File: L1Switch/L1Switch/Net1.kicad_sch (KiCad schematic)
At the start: 66 parts, among them J6 Conn_01x07_Male, U8 VSC8658

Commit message: Most signals routed.
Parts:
- renumbered C206 to C291, C207 to C292, C208 to C293, C209 to C294, C210 to C295, C211 to C296, C212 to C297, C213 to C298, C214 to C299, C215 to C300, C216 to C301, C217 to C302, C218 to C303, C219 to C304, C220 to C305, C221 to C306, C222 to C307, C223 to C308, C224 to C309, C225 to C310, C226 to C311, C227 to C312, C228 to C313, C229 to C314, C230 to C315, C231 to C316, C232 to C317, C233 to C318, C234 to C319, C235 to C320, C236 to C321, C237 to C322, C238 to C323, C239 to C324, C240 to C325, C241 to C326, C242 to C327, C243 to C328, C244 to C329, C245 to C330, C246 to C331, C247 to C332, C248 to C333, C249 to C334, C250 to C335, FB3 to FB4, J6 to J8, R138 to R197, R139 to R198, R140 to R199, R141 to R200, R142 to R201, R143 to R202, R144 to R203, R145 to R204, R146 to R205, R147 to R206, R148 to R207, U8 to U9

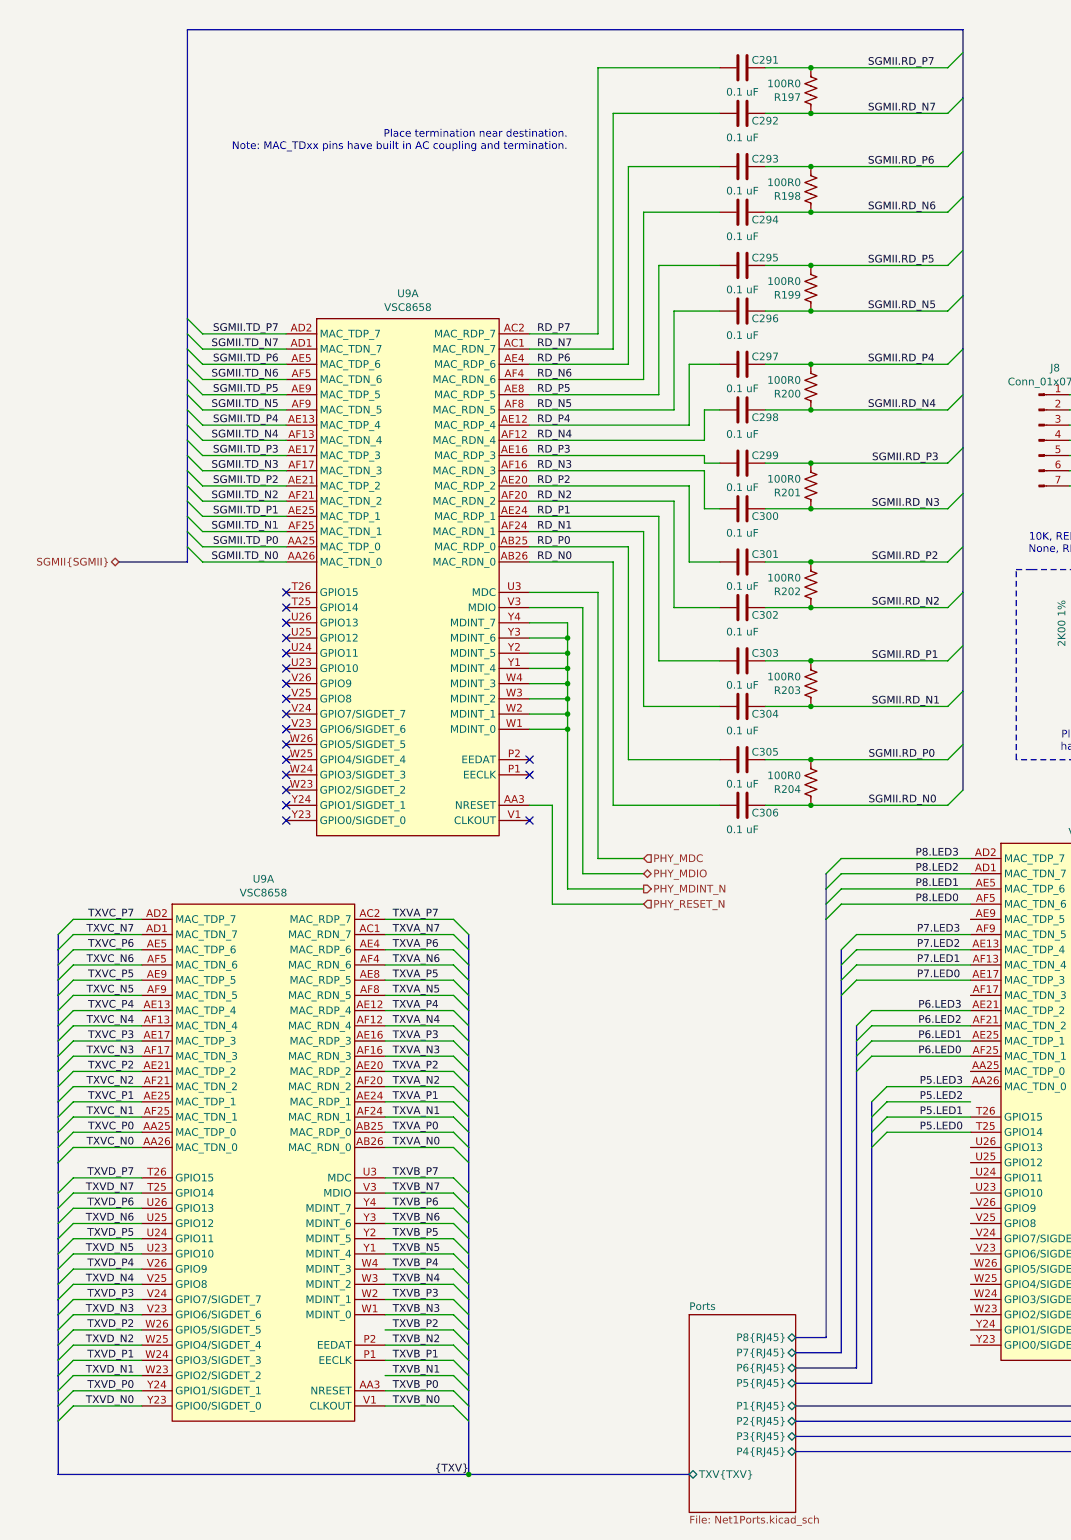
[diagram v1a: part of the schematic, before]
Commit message: Switch to XC7A35T. Update some layout constraints for 4pcb.com capabilities.
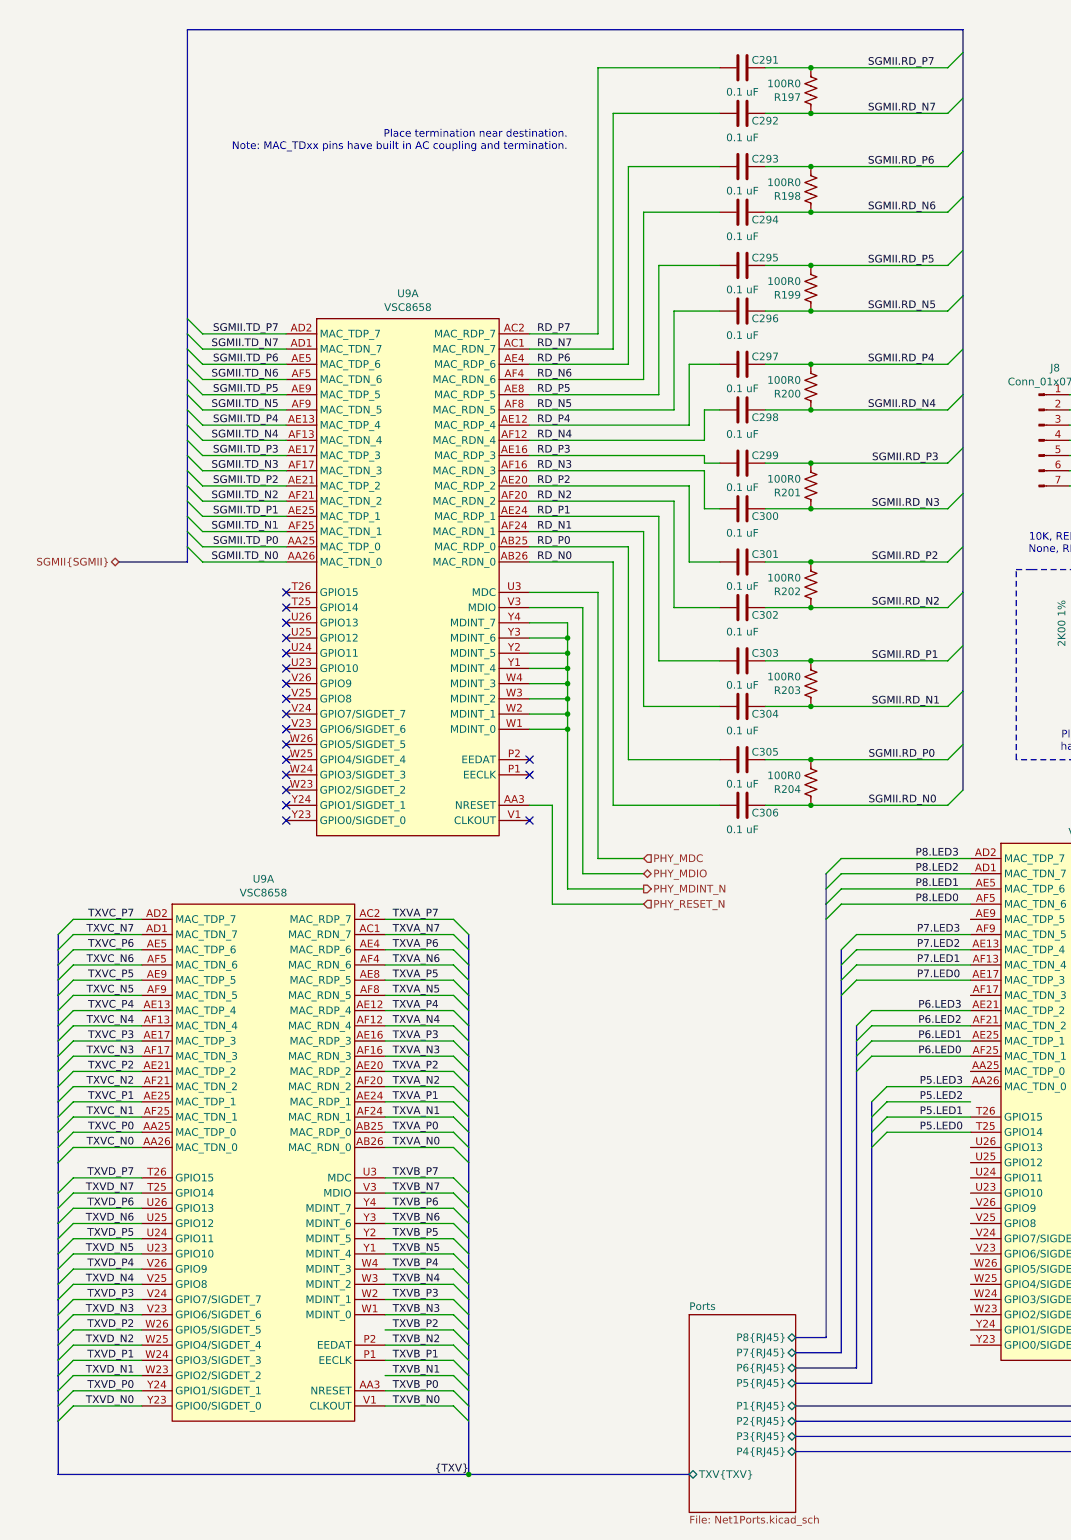
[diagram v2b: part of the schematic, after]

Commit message: Added return path vias. Updated all paths for spacing.
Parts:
- renumbered C291 to C206, C292 to C207, C293 to C208, C294 to C209, C295 to C210, C296 to C211, C297 to C212, C298 to C213, C299 to C214, C300 to C215, C301 to C216, C302 to C217, C303 to C218, C304 to C219, C305 to C220, C306 to C221, C307 to C222, C308 to C223, C309 to C224, C310 to C225, C311 to C226, C312 to C227, C313 to C228, C314 to C229, C315 to C230, C316 to C231, C317 to C232, C318 to C233, C319 to C234, C320 to C235, C321 to C236, C322 to C237, C323 to C238, C324 to C239, C325 to C240, C326 to C241, C327 to C242, C328 to C243, C329 to C244, C330 to C245, C331 to C246, C332 to C247, C333 to C248, C334 to C249, C335 to C250, FB4 to FB3, J8 to J6, R197 to R138, R198 to R139, R199 to R140, R200 to R141, R201 to R142, R202 to R143, R203 to R144, R204 to R145, R205 to R146, R206 to R147, R207 to R148, U9 to U8

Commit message: Added power-on-reset circuit.
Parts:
- renumbered C230 to C100, C231 to C101, C235 to C102, C236 to C103, C237 to C104, C238 to C105, C239 to C106, C240 to C107, C241 to C108, C242 to C109, C206 to C11, C243 to C110, C244 to C111, C245 to C112, C246 to C113, C247 to C114, C248 to C115, C249 to C116, C250 to C117, C232 to C118, C233 to C119, C207 to C12, C234 to C120, C208 to C13, C209 to C14, C210 to C15, C211 to C16, C212 to C17, C213 to C18, C214 to C19, C215 to C20, C216 to C21, C217 to C22, C218 to C23, C219 to C24, C220 to C25, C221 to C26, C222 to C27, C223 to C28, C224 to C94, C225 to C95, C226 to C96, C227 to C97, C228 to C98, C229 to C99, FB3 to FB1, J6 to J2, R139 to R10, R140 to R11, R141 to R12, R142 to R13, R143 to R14, R144 to R15, R145 to R16, R146 to R18, R147 to R19, R148 to R20, R138 to R9, U8 to U2

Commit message: Add FPGA decoupling caps. Add some power planes.
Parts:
- renumbered C11 to C291, C12 to C292, C13 to C293, C14 to C294, C15 to C295, C16 to C296, C17 to C297, C18 to C298, C19 to C299, C20 to C300, C21 to C301, C22 to C302, C23 to C303, C24 to C304, C25 to C305, C26 to C306, C27 to C307, C28 to C308, C94 to C309, C95 to C310, C96 to C311, C97 to C312, C98 to C313, C99 to C314, C100 to C315, C101 to C316, C118 to C317, C119 to C318, C120 to C319, C102 to C320, C103 to C321, C104 to C322, C105 to C323, C106 to C324, C107 to C325, C108 to C326, C109 to C327, C110 to C328, C111 to C329, C112 to C330, C113 to C331, C114 to C332, C115 to C333, C116 to C334, C117 to C335, FB1 to FB4, J2 to J8, R9 to R197, R10 to R198, R11 to R199, R12 to R200, R13 to R201, R14 to R202, R15 to R203, R16 to R204, R18 to R205, R19 to R206, R20 to R207, U2 to U9

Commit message: Add some part info. Fix footprint size for 2kV caps. Add a plane cutout around the magnetics.
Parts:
- C100: renamed from C315; value 100nF -> 100 nF; MFR Part# (none) -> GRM155R71C104KA57D; Manufacturer (none) -> MuRata
- C101: renamed from C316; value 100nF -> 100 nF; MFR Part# (none) -> GRM155R71C104KA57D; Manufacturer (none) -> MuRata
- C102: renamed from C320; value 100nF -> 100 nF; MFR Part# (none) -> GRM155R71C104KA57D; Manufacturer (none) -> MuRata
- C103: renamed from C321; value 100nF -> 100 nF; MFR Part# (none) -> GRM155R71C104KA57D; Manufacturer (none) -> MuRata
- C104: renamed from C322; value 100nF -> 100 nF; MFR Part# (none) -> GRM155R71C104KA57D; Manufacturer (none) -> MuRata
- C105: renamed from C323; value 100nF -> 100 nF; MFR Part# (none) -> GRM155R71C104KA57D; Manufacturer (none) -> MuRata
- C106: renamed from C324; value 100nF -> 100 nF; MFR Part# (none) -> GRM155R71C104KA57D; Manufacturer (none) -> MuRata
- C107: renamed from C325; value 100nF -> 100 nF; MFR Part# (none) -> GRM155R71C104KA57D; Manufacturer (none) -> MuRata
- C108: renamed from C326; value 100nF -> 100 nF; MFR Part# (none) -> GRM155R71C104KA57D; Manufacturer (none) -> MuRata
- C109: renamed from C327; value 100nF -> 100 nF; MFR Part# (none) -> GRM155R71C104KA57D; Manufacturer (none) -> MuRata
- C11: renamed from C291; value 0.1 uF -> 100 nF; MFR Part# (none) -> GRM155R71C104KA57D; Manufacturer (none) -> MuRata
- C110: renamed from C328; value 100nF -> 100 nF; MFR Part# (none) -> GRM155R71C104KA57D; Manufacturer (none) -> MuRata
- C111: renamed from C329; value 100nF -> 100 nF; MFR Part# (none) -> GRM155R71C104KA57D; Manufacturer (none) -> MuRata
- C112: renamed from C330; value 100nF -> 100 nF; MFR Part# (none) -> GRM155R71C104KA57D; Manufacturer (none) -> MuRata
- C113: renamed from C331; value 100nF -> 100 nF; MFR Part# (none) -> GRM155R71C104KA57D; Manufacturer (none) -> MuRata
- C114: renamed from C332; value 100nF -> 100 nF; MFR Part# (none) -> GRM155R71C104KA57D; Manufacturer (none) -> MuRata
- C115: renamed from C333; value 100nF -> 100 nF; MFR Part# (none) -> GRM155R71C104KA57D; Manufacturer (none) -> MuRata
- C116: renamed from C334; value 100nF -> 100 nF; MFR Part# (none) -> GRM155R71C104KA57D; Manufacturer (none) -> MuRata
- C117: renamed from C335; value 100nF -> 100 nF; MFR Part# (none) -> GRM155R71C104KA57D; Manufacturer (none) -> MuRata
- C118: renamed from C317; value 100nF -> 100 nF; MFR Part# (none) -> GRM155R71C104KA57D; Manufacturer (none) -> MuRata
- C119: renamed from C318; value 100nF -> 100 nF; MFR Part# (none) -> GRM155R71C104KA57D; Manufacturer (none) -> MuRata
- C12: renamed from C292; value 0.1 uF -> 100 nF; MFR Part# (none) -> GRM155R71C104KA57D; Manufacturer (none) -> MuRata
- C120: renamed from C319; value 100nF -> 100 nF; MFR Part# (none) -> GRM155R71C104KA57D; Manufacturer (none) -> MuRata
- C13: renamed from C293; value 0.1 uF -> 100 nF; MFR Part# (none) -> GRM155R71C104KA57D; Manufacturer (none) -> MuRata
- C14: renamed from C294; value 0.1 uF -> 100 nF; MFR Part# (none) -> GRM155R71C104KA57D; Manufacturer (none) -> MuRata
- C15: renamed from C295; value 0.1 uF -> 100 nF; MFR Part# (none) -> GRM155R71C104KA57D; Manufacturer (none) -> MuRata
- C16: renamed from C296; value 0.1 uF -> 100 nF; MFR Part# (none) -> GRM155R71C104KA57D; Manufacturer (none) -> MuRata
- C17: renamed from C297; value 0.1 uF -> 100 nF; MFR Part# (none) -> GRM155R71C104KA57D; Manufacturer (none) -> MuRata
- C18: renamed from C298; value 0.1 uF -> 100 nF; MFR Part# (none) -> GRM155R71C104KA57D; Manufacturer (none) -> MuRata
- C19: renamed from C299; value 0.1 uF -> 100 nF; MFR Part# (none) -> GRM155R71C104KA57D; Manufacturer (none) -> MuRata
- C20: renamed from C300; value 0.1 uF -> 100 nF; MFR Part# (none) -> GRM155R71C104KA57D; Manufacturer (none) -> MuRata
- C21: renamed from C301; value 0.1 uF -> 100 nF; MFR Part# (none) -> GRM155R71C104KA57D; Manufacturer (none) -> MuRata
- C22: renamed from C302; value 0.1 uF -> 100 nF; MFR Part# (none) -> GRM155R71C104KA57D; Manufacturer (none) -> MuRata
- C23: renamed from C303; value 0.1 uF -> 100 nF; MFR Part# (none) -> GRM155R71C104KA57D; Manufacturer (none) -> MuRata
- C24: renamed from C304; value 0.1 uF -> 100 nF; MFR Part# (none) -> GRM155R71C104KA57D; Manufacturer (none) -> MuRata
- C25: renamed from C305; value 0.1 uF -> 100 nF; MFR Part# (none) -> GRM155R71C104KA57D; Manufacturer (none) -> MuRata
- C26: renamed from C306; value 0.1 uF -> 100 nF; MFR Part# (none) -> GRM155R71C104KA57D; Manufacturer (none) -> MuRata
- C27: renamed from C307; MFR Part# (none) -> GRM188B11A105KA61D; Manufacturer (none) -> MuRata
- C28: renamed from C308; MFR Part# (none) -> GRM188B11A105KA61D; Manufacturer (none) -> MuRata
- C94: renamed from C309; value 100nF -> 100 nF; MFR Part# (none) -> GRM155R71C104KA57D; Manufacturer (none) -> MuRata
- C95: renamed from C310; value 100nF -> 100 nF; MFR Part# (none) -> GRM155R71C104KA57D; Manufacturer (none) -> MuRata
- C96: renamed from C311; value 100nF -> 100 nF; MFR Part# (none) -> GRM155R71C104KA57D; Manufacturer (none) -> MuRata
- C97: renamed from C312; value 100nF -> 100 nF; MFR Part# (none) -> GRM155R71C104KA57D; Manufacturer (none) -> MuRata
- C98: renamed from C313; value 100nF -> 100 nF; MFR Part# (none) -> GRM155R71C104KA57D; Manufacturer (none) -> MuRata
- C99: renamed from C314; value 100nF -> 100 nF; MFR Part# (none) -> GRM155R71C104KA57D; Manufacturer (none) -> MuRata
- FB1: renamed from FB4; MFR Part# (none) -> BLM31PG121SH1L; Manufacturer (none) -> MuRata
- J2: renamed from J8; MFR Part# (none) -> 68000-107HLF; Manufacturer (none) -> Amphenol
- U2: renamed from U9; MFR Part# (none) -> VSC8658XHJ; Manufacturer (none) -> Microchip Technology
- renumbered R198 to R10, R199 to R11, R200 to R12, R201 to R13, R202 to R14, R203 to R15, R204 to R16, R205 to R18, R206 to R19, R207 to R20, R197 to R9

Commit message: Update part numbers.
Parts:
- C291: renamed from C11; MFR Part# GRM155R71C104KA57D -> GRM155R71C104KA88D
- C292: renamed from C12; MFR Part# GRM155R71C104KA57D -> GRM155R71C104KA88D
- C293: renamed from C13; MFR Part# GRM155R71C104KA57D -> GRM155R71C104KA88D
- C294: renamed from C14; MFR Part# GRM155R71C104KA57D -> GRM155R71C104KA88D
- C295: renamed from C15; MFR Part# GRM155R71C104KA57D -> GRM155R71C104KA88D
- C296: renamed from C16; MFR Part# GRM155R71C104KA57D -> GRM155R71C104KA88D
- C297: renamed from C17; MFR Part# GRM155R71C104KA57D -> GRM155R71C104KA88D
- C298: renamed from C18; MFR Part# GRM155R71C104KA57D -> GRM155R71C104KA88D
- C299: renamed from C19; MFR Part# GRM155R71C104KA57D -> GRM155R71C104KA88D
- C300: renamed from C20; MFR Part# GRM155R71C104KA57D -> GRM155R71C104KA88D
- C301: renamed from C21; MFR Part# GRM155R71C104KA57D -> GRM155R71C104KA88D
- C302: renamed from C22; MFR Part# GRM155R71C104KA57D -> GRM155R71C104KA88D
- C303: renamed from C23; MFR Part# GRM155R71C104KA57D -> GRM155R71C104KA88D
- C304: renamed from C24; MFR Part# GRM155R71C104KA57D -> GRM155R71C104KA88D
- C305: renamed from C25; MFR Part# GRM155R71C104KA57D -> GRM155R71C104KA88D
- C306: renamed from C26; MFR Part# GRM155R71C104KA57D -> GRM155R71C104KA88D
- C309: renamed from C94; MFR Part# GRM155R71C104KA57D -> GRM155R71C104KA88D
- C310: renamed from C95; MFR Part# GRM155R71C104KA57D -> GRM155R71C104KA88D
- C311: renamed from C96; MFR Part# GRM155R71C104KA57D -> GRM155R71C104KA88D
- C312: renamed from C97; MFR Part# GRM155R71C104KA57D -> GRM155R71C104KA88D
- C313: renamed from C98; MFR Part# GRM155R71C104KA57D -> GRM155R71C104KA88D
- C314: renamed from C99; MFR Part# GRM155R71C104KA57D -> GRM155R71C104KA88D
- C315: renamed from C100; MFR Part# GRM155R71C104KA57D -> GRM155R71C104KA88D
- C316: renamed from C101; MFR Part# GRM155R71C104KA57D -> GRM155R71C104KA88D
- C317: renamed from C118; MFR Part# GRM155R71C104KA57D -> GRM155R71C104KA88D
- C318: renamed from C119; MFR Part# GRM155R71C104KA57D -> GRM155R71C104KA88D
- C319: renamed from C120; MFR Part# GRM155R71C104KA57D -> GRM155R71C104KA88D
- C320: renamed from C102; MFR Part# GRM155R71C104KA57D -> GRM155R71C104KA88D
- C321: renamed from C103; MFR Part# GRM155R71C104KA57D -> GRM155R71C104KA88D
- C322: renamed from C104; MFR Part# GRM155R71C104KA57D -> GRM155R71C104KA88D
- C323: renamed from C105; MFR Part# GRM155R71C104KA57D -> GRM155R71C104KA88D
- C324: renamed from C106; MFR Part# GRM155R71C104KA57D -> GRM155R71C104KA88D
- C325: renamed from C107; MFR Part# GRM155R71C104KA57D -> GRM155R71C104KA88D
- C326: renamed from C108; MFR Part# GRM155R71C104KA57D -> GRM155R71C104KA88D
- C327: renamed from C109; MFR Part# GRM155R71C104KA57D -> GRM155R71C104KA88D
- C328: renamed from C110; MFR Part# GRM155R71C104KA57D -> GRM155R71C104KA88D
- C329: renamed from C111; MFR Part# GRM155R71C104KA57D -> GRM155R71C104KA88D
- C330: renamed from C112; MFR Part# GRM155R71C104KA57D -> GRM155R71C104KA88D
- C331: renamed from C113; MFR Part# GRM155R71C104KA57D -> GRM155R71C104KA88D
- C332: renamed from C114; MFR Part# GRM155R71C104KA57D -> GRM155R71C104KA88D
- C333: renamed from C115; MFR Part# GRM155R71C104KA57D -> GRM155R71C104KA88D
- C334: renamed from C116; MFR Part# GRM155R71C104KA57D -> GRM155R71C104KA88D
- C335: renamed from C117; MFR Part# GRM155R71C104KA57D -> GRM155R71C104KA88D
- R197: renamed from R9; MFR Part# (none) -> RC0402FR-13100RL; Manufacturer (none) -> Yageo
- R198: renamed from R10; MFR Part# (none) -> RC0402FR-13100RL; Manufacturer (none) -> Yageo
- R199: renamed from R11; MFR Part# (none) -> RC0402FR-13100RL; Manufacturer (none) -> Yageo
- R200: renamed from R12; MFR Part# (none) -> RC0402FR-13100RL; Manufacturer (none) -> Yageo
- R201: renamed from R13; MFR Part# (none) -> RC0402FR-13100RL; Manufacturer (none) -> Yageo
- R202: renamed from R14; MFR Part# (none) -> RC0402FR-13100RL; Manufacturer (none) -> Yageo
- R203: renamed from R15; MFR Part# (none) -> RC0402FR-13100RL; Manufacturer (none) -> Yageo
- R204: renamed from R16; MFR Part# (none) -> RC0402FR-13100RL; Manufacturer (none) -> Yageo
- R205: renamed from R18; value 2K00 1% -> 2K0; MFR Part# (none) -> RC0603FR-132KL; Manufacturer (none) -> Yageo
- R206: renamed from R19; value 2K00 1% -> 2K0; MFR Part# (none) -> RC0603FR-132KL; Manufacturer (none) -> Yageo
- R207: renamed from R20; value 10K -> 10K0; MFR Part# (none) -> CRCW040210K0FKED; Manufacturer (none) -> Vishay
- renumbered C27 to C307, C28 to C308, FB1 to FB4, J2 to J8, U2 to U9
